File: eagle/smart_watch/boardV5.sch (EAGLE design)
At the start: 67 parts, among them IC1 SC16IS750, U1 MCP73831, U2 TPS61200, U3 MAX1704X, U4 V_REG_LDOSMD, Y1 16MHz, Y2 12.28MHz

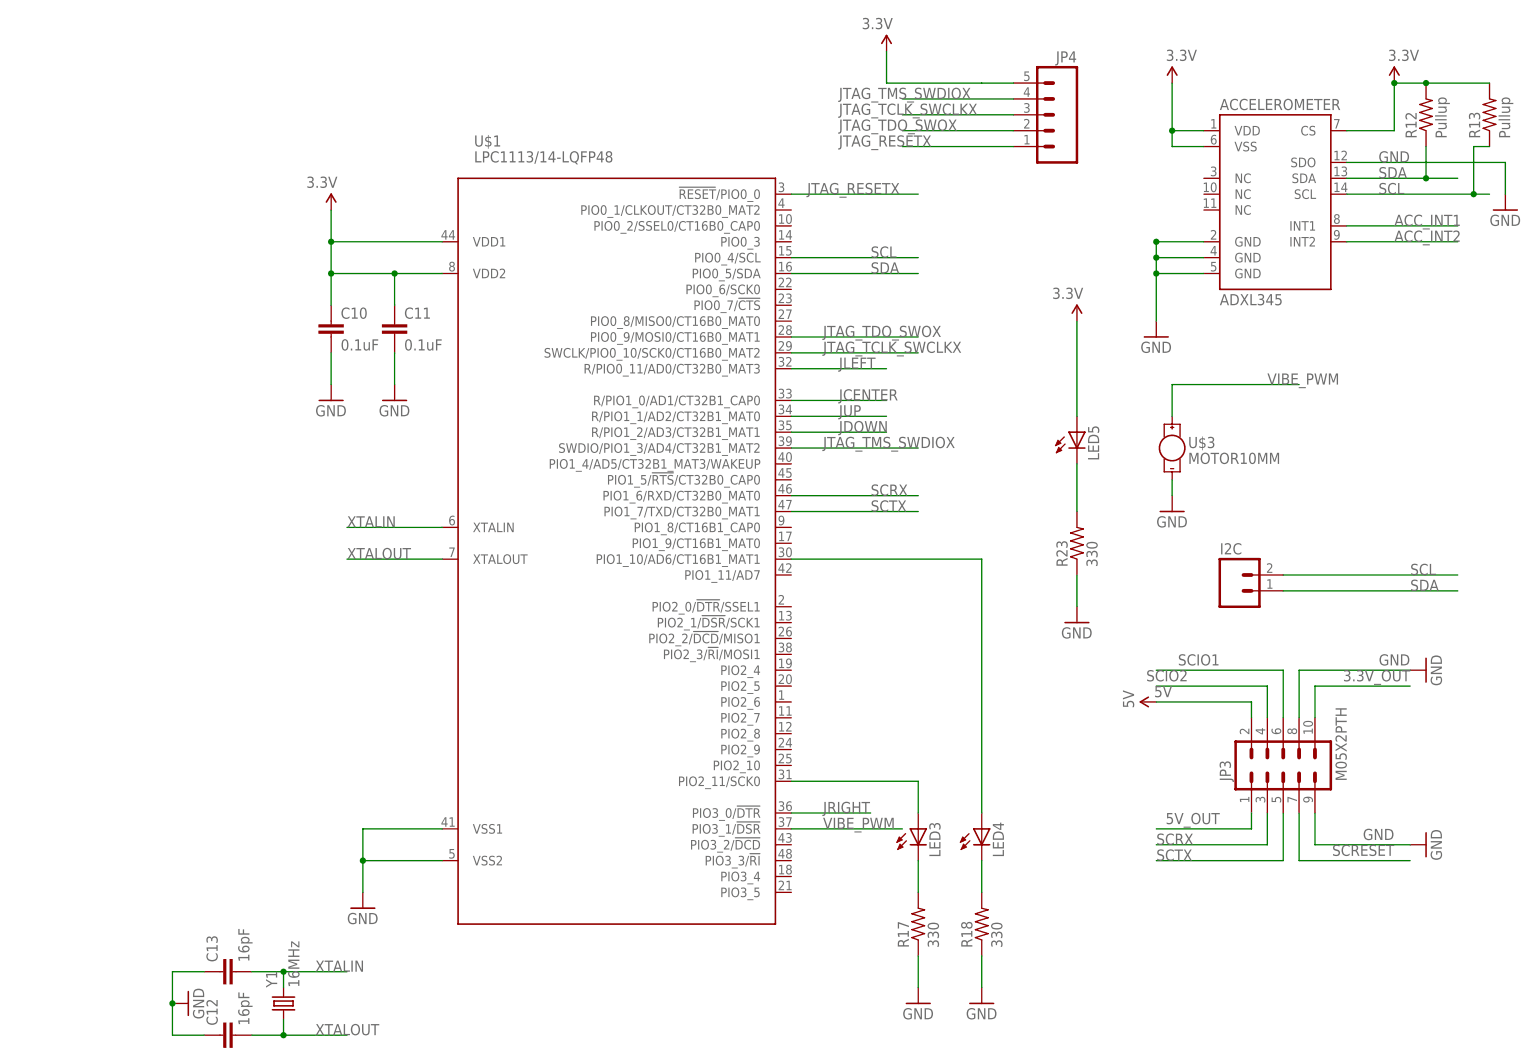
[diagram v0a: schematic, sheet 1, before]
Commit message: Made a few minor changes to board V4, added V5 with edits for printing. TODO: Wiring of board V5. See email for other additions
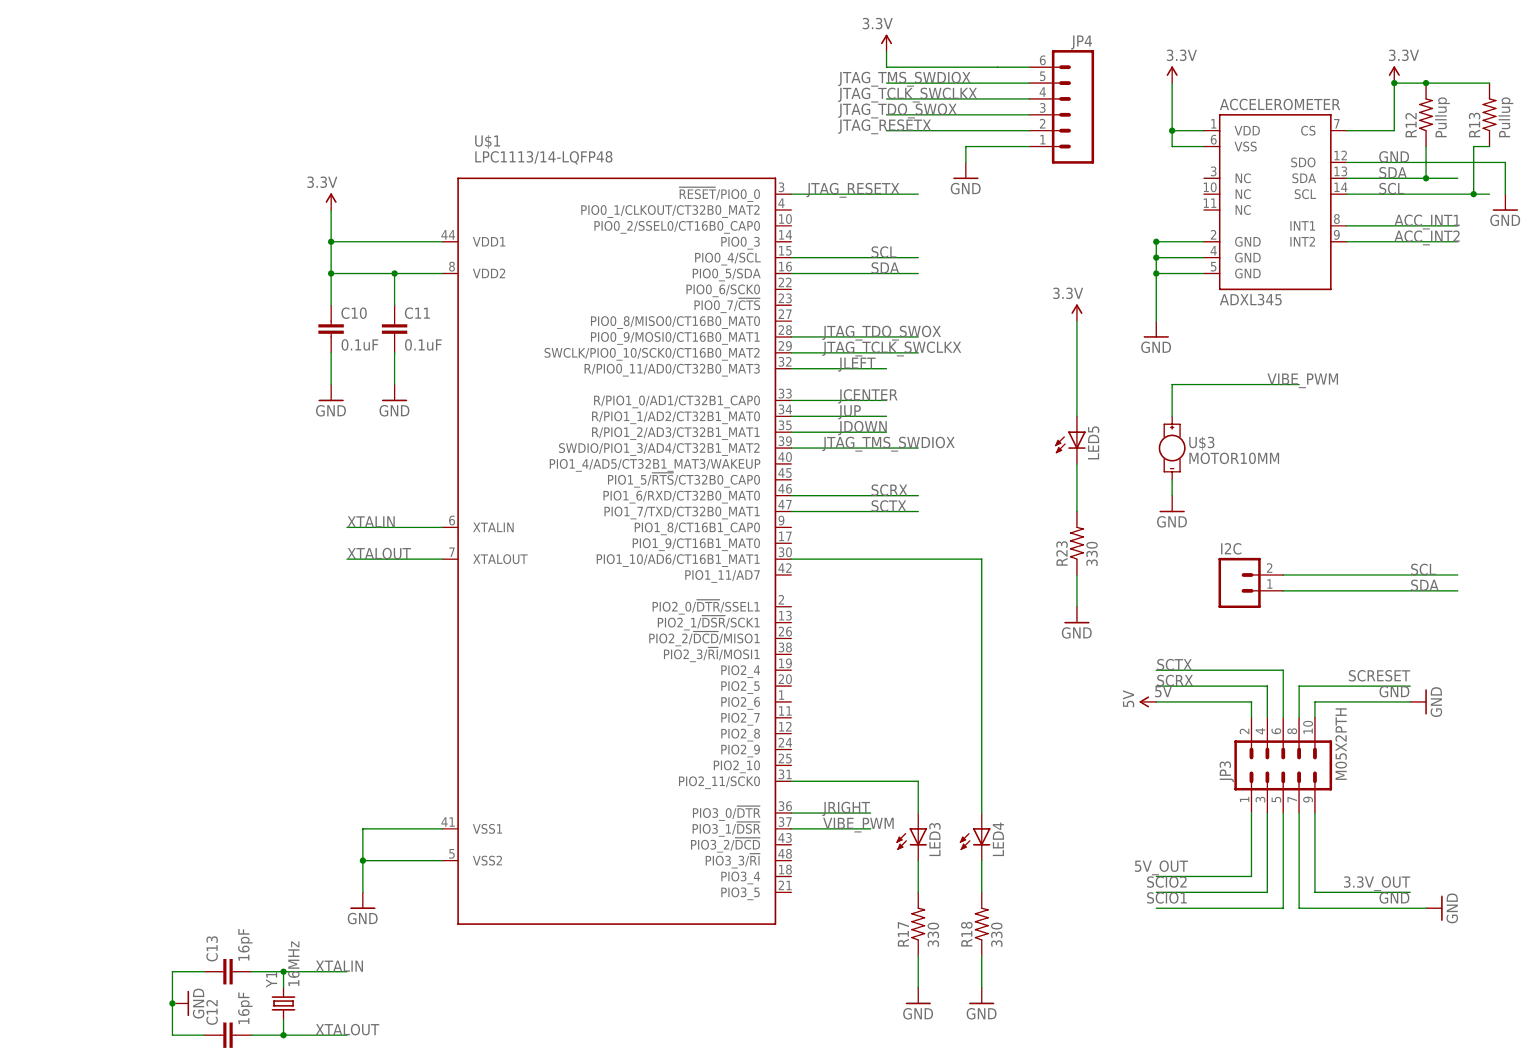
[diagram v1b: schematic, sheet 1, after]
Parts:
- removed JP5, JP6: (no value), SparkFun-Connectors:M07
- removed R1, R19, R20, R21, R22: 10k, SparkFun-Resistors:RESISTOR0603-RES
- removed S1: (no value), SparkFun-Electromechanical:JOYSTICK_MINI
- added S2: (no value), SparkFun-Electromechanical:SWITCH-SPDT-SMD-A
- JP4: device SparkFun-Connectors:M05PTH -> SparkFun-Connectors:M06POLAR
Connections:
- new net N$14: C2.1, S2.O, U1.VBAT
- new net N$26: JP2.2, S2.P
- net 3.3V: now also JP4.6; no longer JP4.5, JP5.7, JP6.7, R1.1, R19.1, R20.1, R21.1, R22.1
- net 3.3V_OUT: now also JP3.9; no longer JP3.10
- net GND: now also JP3.10, JP3.7, JP4.1; no longer JP3.8, JP3.9, JP5.5, JP6.5, S1.GND
- net JCENTER: no longer JP5.2, JP6.2, R22.2, S1.CENT
- net JDOWN: no longer JP5.4, JP6.4, R1.2, S1.DOWN
- net JLEFT: no longer JP5.1, JP6.1, R20.2, S1.LEFT
- net JRIGHT: no longer JP5.6, JP6.6, R21.2, S1.RIGHT
- net JTAG_RESETX: now also JP4.2; no longer JP4.1
- net JTAG_TCLK_SWCLKX: now also JP4.4; no longer JP4.3
- net JTAG_TDO_SWOX: now also JP4.3; no longer JP4.2
- net JTAG_TMS_SWDIOX: now also JP4.5; no longer JP4.4
- net JUP: no longer JP5.3, JP6.3, R19.2, S1.UP
- net SCIO1: now also JP3.5; no longer JP3.6
- net SCIO2: now also JP3.3; no longer JP3.4
- net SCRESET: now also JP3.8; no longer JP3.7
- net SCRX: now also JP3.4; no longer JP3.3
- net SCTX: now also JP3.6; no longer JP3.5
- net VBATT: now also S2.S; no longer C2.1, JP2.2, U1.VBAT
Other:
- moved on the sheet: C2, JP2

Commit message: Git commit. Finished and printed board V5
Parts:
- added JP5: (no value), SparkFun-Connectors:M07
- added R1: 12k, SparkFun-Passives:RESISTOR0603-RES
- added R16: 1k, SparkFun-Passives:RESISTOR0603-RES
- Y2: value 12.28MHz -> 14.7456MHz
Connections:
- removed net N$1: IC1./IRQ, R14.1
- new net BATINT: R16.2, U$1.PIO2_5, U3.ALT
- new net IRQB: IC1./IRQ, R14.1, U$1.PIO2_6
- net 3.3V: now also IC1.A0-/CS, IC1.A1-SI, JP5.7, R1.2, R16.1
- net GND: now also JP3.8, JP5.5, Y1.GND, Y2.GND; no longer IC1.A0-/CS, IC1.A1-SI, JP3.10
- net JCENTER: now also JP5.2
- net JDOWN: now also JP5.4
- net JLEFT: now also JP5.1
- net JRIGHT: now also JP5.6
- net JTAG_RESETX: now also R1.1
- net JUP: now also JP5.3
- net SCRESET: now also JP3.10; no longer JP3.8
- net VIBE_PWM: now also U$1.PIO2_3/!RI!/MOSI1
